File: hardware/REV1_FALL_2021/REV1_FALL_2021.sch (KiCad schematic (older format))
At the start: 5 parts

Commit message: Added annotationsto circuits
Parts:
- gave numbers to parts that had none: 5
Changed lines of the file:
@@
 $EndDescr
 $Comp
-L teensy:Teensy3.6_All_Pins U?
+L teensy:Teensy3.6_All_Pins U1
 U 1 1 6198EEB0
 P 2200 3600
-F 0 "U?" H 2200 6237 60  0000 C CNN
+F 0 "U1" H 2200 6237 60  0000 C CNN
 F 1 "Teensy3.6_All_Pins" H 2200 6131 60  0000 C CNN
 F 2 "teensy:Teensy35_36" H 2200 3650 60  0000 C CNN
@@
 $EndComp
 $Comp
-L REV1_FALL_2021-rescue:BNO055_Breakout-Sensors_2021_2022 U?
+L REV1_FALL_2021-rescue:BNO055_Breakout-Sensors_2021_2022 U4
 U 1 1 61992B5E
 P 5950 2000
-F 0 "U?" H 5950 2800 50  0000 C CNN
+F 0 "U4" H 5950 2800 50  0000 C CNN
 F 1 "BNO055_Breakout" H 5950 2700 50  0000 C CNN
 F 2 "sensors_2021_2022:BNO055_Breakout" H 5950 2750 50  0001 C CNN
@@
 $EndComp
 $Comp
-L Sensors_2021_2022:MPL3115A2_Breakout U?
+L Sensors_2021_2022:MPL3115A2_Breakout U3
 U 1 1 61994643
 P 5900 3950
-F 0 "U?" H 5850 4750 50  0000 L CNN
+F 0 "U3" H 5850 4750 50  0000 L CNN
 F 1 "MPL3115A2_Breakout" H 5500 4850 50  0000 L CNN
 F 2 "sensors_2021_2022:MPL311A2_Breakout" H 5900 4400 50  0001 C CNN
@@
 $EndComp
 $Comp
-L Sensors_2021_2022:PA16165_Breakout U?
+L Sensors_2021_2022:PA16165_Breakout U2
 U 1 1 6199B8C8
 P 5850 6000
-F 0 "U?" H 5800 6950 50  0000 L CNN
+F 0 "U2" H 5800 6950 50  0000 L CNN
 F 1 "PA16165_Breakout" H 5500 7050 50  0000 L CNN
 F 2 "sensors_2021_2022:PA16165_Breakout" H 5800 6650 50  0001 C CNN
@@
 $EndComp
 $Comp
-L Sensors_2021_2022:RFM69HCW_Breakout U?
+L Sensors_2021_2022:RFM69HCW_Breakout U5
 U 1 1 6194AAD4
 P 9050 2250
-F 0 "U?" H 9050 3298 50  0000 C CNN
+F 0 "U5" H 9050 3298 50  0000 C CNN
 F 1 "RFM69HCW_Breakout" H 9050 3207 50  0000 C CNN
 F 2 "sensors_2021_2022:RFM69HCW_Breakout" H 8900 3050 50  0001 C CNN

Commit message: Added outlines on the breakout board's footprints. Assembled PCB with wires, needs checking by Ian
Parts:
- U3: footprint sensors_2021_2022:MPL311A2_Breakout -> sensors_2021_2022:MPL3115A2_Breakout
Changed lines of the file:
@@
 F 0 "U3" H 5850 4750 50  0000 L CNN
 F 1 "MPL3115A2_Breakout" H 5500 4850 50  0000 L CNN
-F 2 "sensors_2021_2022:MPL311A2_Breakout" H 5900 4400 50  0001 C CNN
+F 2 "sensors_2021_2022:MPL3115A2_Breakout" H 5900 4400 50  0001 C CNN
 F 3 "" H 5900 4400 50  0001 C CNN
 	1    5900 3950
@@
 F 3 "" H 5800 6650 50  0001 C CNN
 	1    5850 6000
-	1    0    0    -1
-$EndComp
-$Comp
-L Sensors_2021_2022:RFM69HCW_Breakout U5
-U 1 1 6194AAD4
-P 9050 2250
-F 0 "U5" H 9050 3298 50  0000 C CNN
-F 1 "RFM69HCW_Breakout" H 9050 3207 50  0000 C CNN
-F 2 "sensors_2021_2022:RFM69HCW_Breakout" H 8900 3050 50  0001 C CNN
-F 3 "" H 8900 3050 50  0001 C CNN
-	1    9050 2250
 	1    0    0    -1
 $EndComp
@@
 NoConn ~ 9400 1800
 NoConn ~ 9400 1650
+$Comp
+L Sensors_2021_2022:RFM69HCW_Breakout U5
+U 1 1 6194AAD4
+P 9050 2250
+F 0 "U5" H 9050 3298 50  0000 C CNN
+F 1 "RFM69HCW_Breakout" H 9050 3207 50  0000 C CNN
+F 2 "sensors_2021_2022:RFM69HCW_Breakout" H 8900 3050 50  0001 C CNN
+F 3 "" H 8900 3050 50  0001 C CNN
+	1    9050 2250
+	1    0    0    -1
+$EndComp
 $EndSCHEMATC

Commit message: Verify pin connections on layout and fix mistakes
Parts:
- U4: symbol REV1_FALL_2021-rescue:BNO055_Breakout-Sensors_2021_2022 -> Sensors_2021_2022:BNO055_Breakout
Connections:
- wire segments 32 -> 36
- no-connect marks 96 -> 91
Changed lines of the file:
@@
 $EndComp
 $Comp
-L REV1_FALL_2021-rescue:BNO055_Breakout-Sensors_2021_2022 U4
+L Sensors_2021_2022:BNO055_Breakout U4
 U 1 1 61992B5E
 P 5950 2000
@@
 	1    0    0    -1
 $EndComp
-$Comp
-L Sensors_2021_2022:PA16165_Breakout U2
-U 1 1 6199B8C8
-P 5850 6000
-F 0 "U2" H 5800 6950 50  0000 L CNN
-F 1 "PA16165_Breakout" H 5500 7050 50  0000 L CNN
-F 2 "sensors_2021_2022:PA16165_Breakout" H 5800 6650 50  0001 C CNN
-F 3 "" H 5800 6650 50  0001 C CNN
-	1    5850 6000
-	1    0    0    -1
-$EndComp
-Text Label 3650 2550 0    50   ~ 0
+Text Label 3600 5150 0    50   ~ 0
 3.3V
 Text Label 5300 1650 0    50   ~ 0
@@
 Text Label 5350 3500 0    50   ~ 0
 3.3V
-Text Label 5300 5400 0    50   ~ 0
+Text Label 5300 6450 0    50   ~ 0
 3.3V
 Text Label 8400 1650 0    50   ~ 0
 3.3V
-Text Label 3650 2650 0    50   ~ 0
-GND
-Text Label 5300 1800 0    50   ~ 0
+Text Label 900  5250 2    50   ~ 0
+GND
+Text Label 5300 1950 0    50   ~ 0
 GND
 Text Label 5350 3650 0    50   ~ 0
@@
 Text Label 5350 4400 0    50   ~ 0
 SDA0
+Text Label 5300 2100 0    50   ~ 0
+SDA0
 Text Label 5300 2250 0    50   ~ 0
-SDA0
-Text Label 5300 2100 0    50   ~ 0
 SCL0
 Text Label 5350 4250 0    50   ~ 0
@@
 	5600 1650 5300 1650
 Wire Wire Line
-	5300 1800 5600 1800
-Wire Wire Line
 	5600 2100 5300 2100
 Wire Wire Line
@@
 	5650 4400 5350 4400
 Wire Wire Line
-	5300 5400 5600 5400
-Wire Wire Line
 	5600 6000 5300 6000
 Wire Wire Line
@@
 Wire Wire Line
 	8400 2850 8700 2850
-NoConn ~ 1050 1450
 NoConn ~ 1050 1950
 NoConn ~ 1050 2050
@@
 NoConn ~ 1050 2350
 NoConn ~ 1050 2450
-NoConn ~ 1050 2850
 NoConn ~ 1050 2950
 NoConn ~ 1050 3050
@@
 NoConn ~ 1050 5050
 NoConn ~ 1050 5150
-NoConn ~ 1050 5250
 NoConn ~ 1050 5450
 NoConn ~ 1050 5550
@@
 NoConn ~ 3350 5350
 NoConn ~ 3350 5250
-NoConn ~ 3350 5150
 NoConn ~ 3350 5050
 NoConn ~ 3350 4950
@@
 NoConn ~ 6300 2100
 NoConn ~ 6300 2250
-NoConn ~ 5600 1950
 NoConn ~ 5600 2400
 NoConn ~ 5650 3800
@@
 NoConn ~ 5600 5700
 NoConn ~ 5600 5850
-NoConn ~ 5600 6450
 NoConn ~ 5600 6600
 NoConn ~ 8700 1950
@@
 	1    0    0    -1
 $EndComp
+$Comp
+L Sensors_2021_2022:PA16165_Breakout U2
+U 1 1 6199B8C8
+P 5850 6000
+F 0 "U2" H 5800 6950 50  0000 L CNN
+F 1 "PA16165_Breakout" H 5500 7050 50  0000 L CNN
+F 2 "sensors_2021_2022:PA16165_Breakout" H 5800 6650 50  0001 C CNN
+F 3 "" H 5800 6650 50  0001 C CNN
+	1    5850 6000
+	1    0    0    -1
+$EndComp
+Wire Wire Line
+	5600 6450 5300 6450
+NoConn ~ 5600 5400
+Wire Wire Line
+	5600 1950 5300 1950
+Wire Wire Line
+	3350 5150 3600 5150
+Wire Wire Line
+	1050 5250 900  5250
+Text Label 900  1450 2    50   ~ 0
+GND
+Wire Wire Line
+	1050 1450 900  1450
+Text Label 750  2850 0    50   ~ 0
+3.3V
+Wire Wire Line
+	1050 2850 750  2850
 $EndSCHEMATC

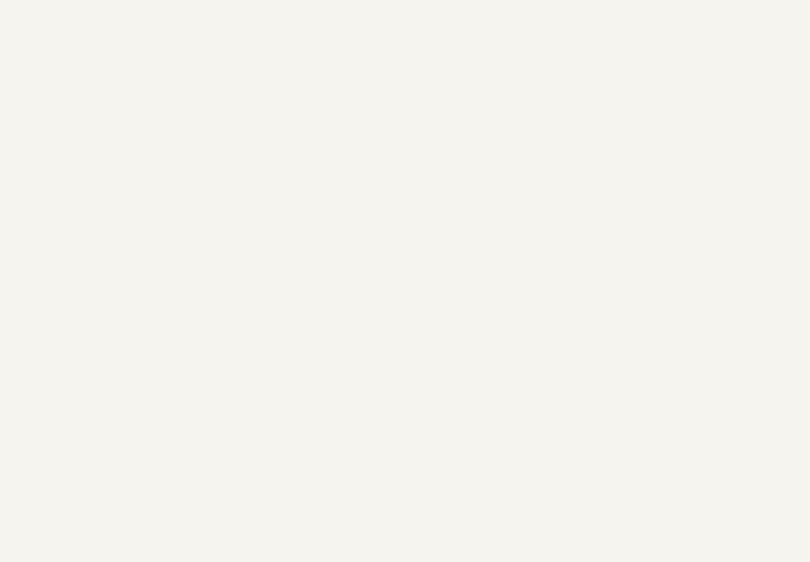
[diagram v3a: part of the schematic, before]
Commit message: add power switcher (no traces connected yet)
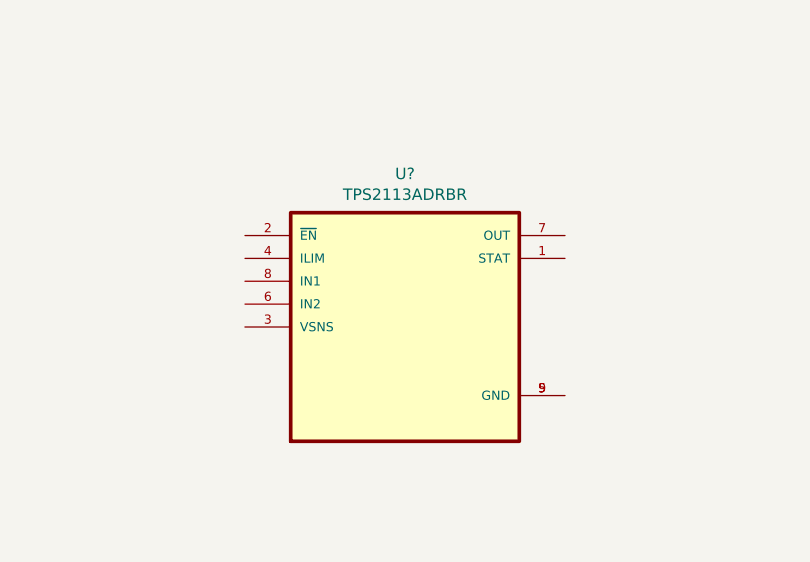
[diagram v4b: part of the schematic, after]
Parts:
- added U?: TPS2113ADRBR, IC_DRV8601DRBT, symbol TPS2113ADRBR:TPS2113ADRBR
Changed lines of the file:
@@
 Wire Wire Line
 	1050 2850 750  2850
+$Comp
+L TPS2113ADRBR:TPS2113ADRBR U?
+U 1 1 6198C58A
+P 9550 5800
+F 0 "U?" H 9550 6470 50  0000 C CNN
+F 1 "TPS2113ADRBR" H 9550 6379 50  0000 C CNN
+F 2 "IC_DRV8601DRBT" H 9550 5800 50  0001 L BNN
+F 3 "" H 9550 5800 50  0001 L BNN
+	1    9550 5800
+	1    0    0    -1
+$EndComp
 $EndSCHEMATC

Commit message: WIP adding TPS2113A
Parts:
- added BT? (x2): Battery_Cell, symbol Device:Battery_Cell
- added C? (x2): C, symbol Device:C
- added R? (x2): R, symbol Device:R
- added R?: 15k, symbol Device:R
- added R?: 5k, symbol Device:R
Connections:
- net labels added: SWITCH, VIN
- wire segments 36 -> 76
- no-connect marks 91 -> 89
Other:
- moved on the sheet: U?

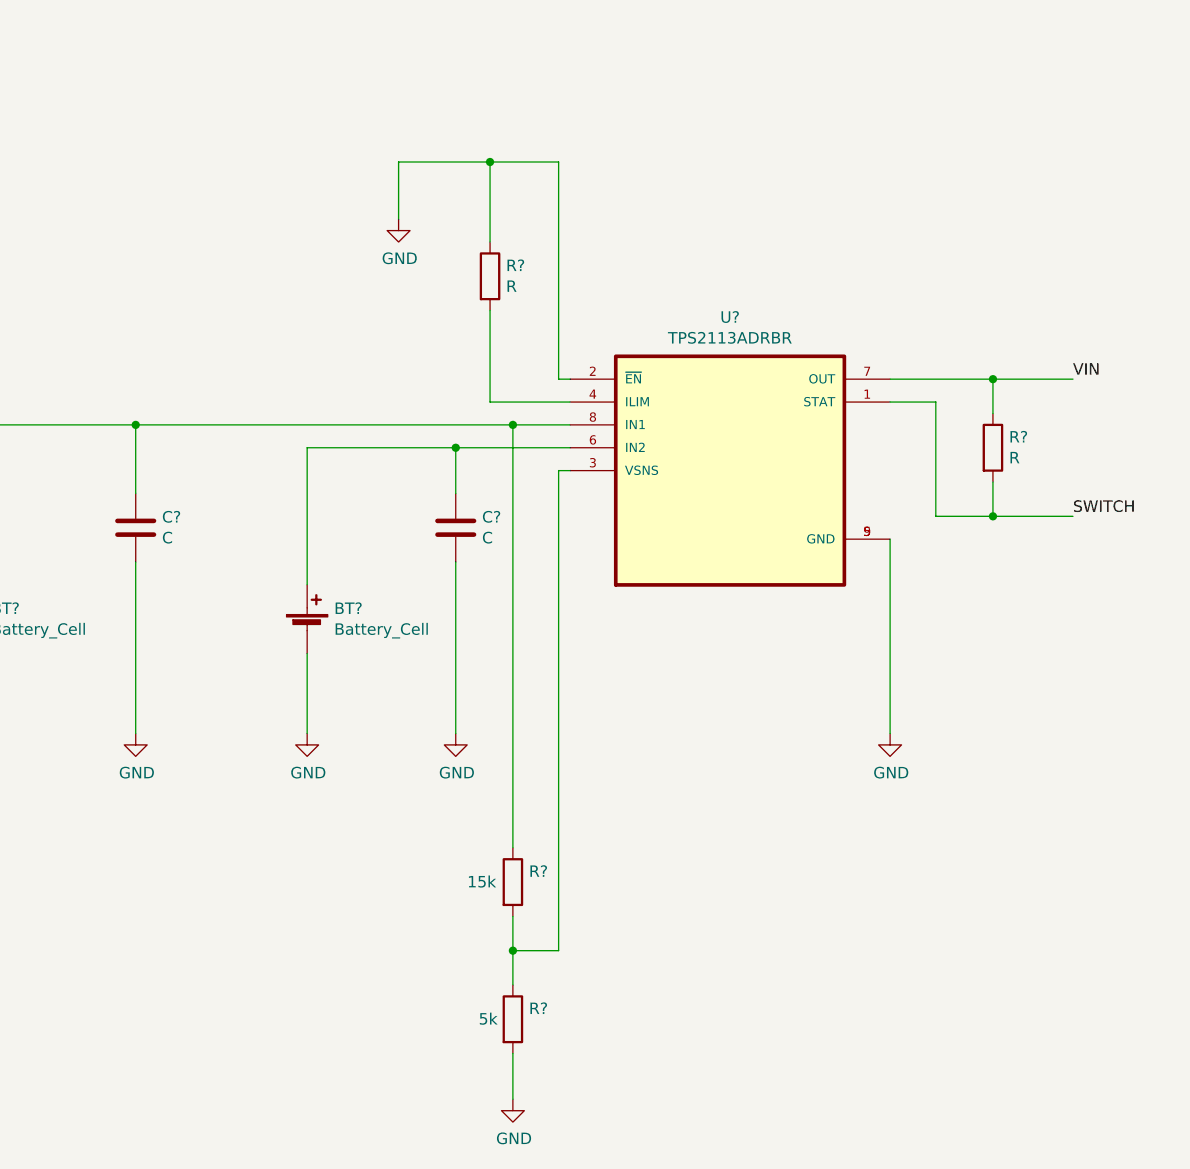
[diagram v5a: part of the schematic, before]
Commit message: finish TPS2113A schematic
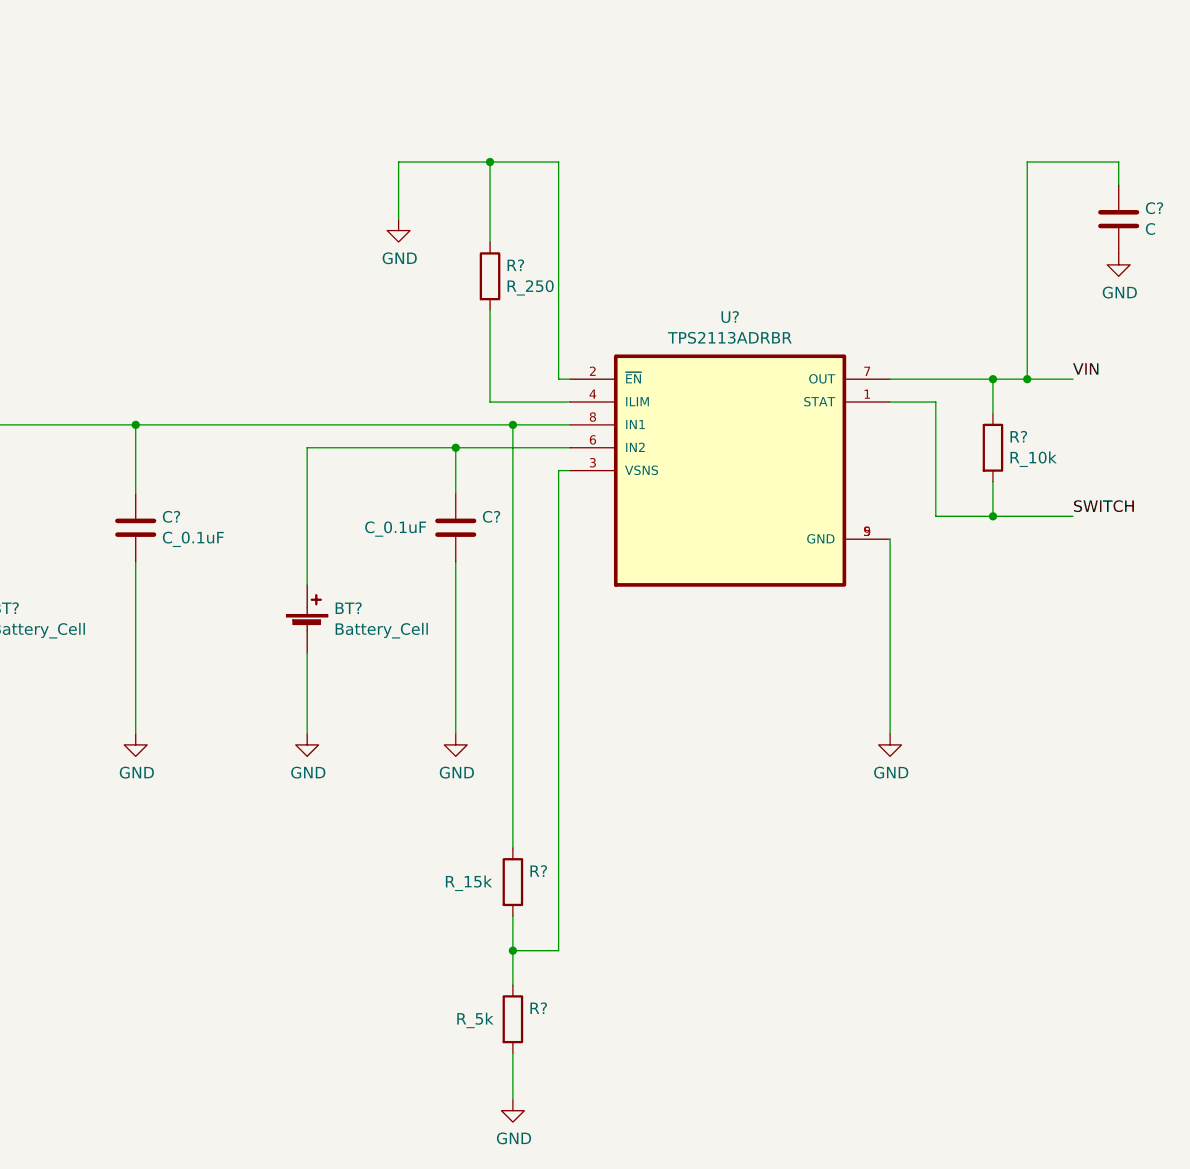
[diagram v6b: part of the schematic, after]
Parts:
- added C?: C, symbol Device:C
- C? (x2): value C -> C_0.1uF
- R?: value R -> R_250
- R?: value 15k -> R_15k
- R?: value 5k -> R_5k
- R?: value R -> R_10k
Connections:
- net GND: now also C?.2
- net VIN: now also C?.1
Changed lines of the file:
@@
 P 13750 5600
 F 0 "C?" H 13865 5646 50  0000 L CNN
-F 1 "C" H 13865 5555 50  0000 L CNN
+F 1 "C_0.1uF" H 13865 5555 50  0000 L CNN
 F 2 "" H 13788 5450 50  0001 C CNN
 F 3 "~" H 13750 5600 50  0001 C CNN
@@
 P 15150 5600
 F 0 "C?" H 15265 5646 50  0000 L CNN
-F 1 "C" H 15265 5555 50  0000 L CNN
+F 1 "C_0.1uF" H 14750 5600 50  0000 L CNN
 F 2 "" H 15188 5450 50  0001 C CNN
 F 3 "~" H 15150 5600 50  0001 C CNN
@@
 P 15300 4500
 F 0 "R?" H 15370 4546 50  0000 L CNN
-F 1 "R" H 15370 4455 50  0000 L CNN
+F 1 "R_250" H 15370 4455 50  0000 L CNN
 F 2 "" V 15230 4500 50  0001 C CNN
 F 3 "~" H 15300 4500 50  0001 C CNN
@@
 P 15400 7150
 F 0 "R?" H 15470 7196 50  0000 L CNN
-F 1 "15k" H 15200 7150 50  0000 L CNN
+F 1 "R_15k" H 15100 7150 50  0000 L CNN
 F 2 "" V 15330 7150 50  0001 C CNN
 F 3 "~" H 15400 7150 50  0001 C CNN
@@
 P 15400 7750
 F 0 "R?" H 15470 7796 50  0000 L CNN
-F 1 "5k" H 15250 7750 50  0000 L CNN
+F 1 "R_5k" H 15150 7750 50  0000 L CNN
 F 2 "" V 15330 7750 50  0001 C CNN
 F 3 "~" H 15400 7750 50  0001 C CNN
@@
 P 17500 5250
 F 0 "R?" H 17570 5296 50  0000 L CNN
-F 1 "R" H 17570 5205 50  0000 L CNN
+F 1 "R_10k" H 17570 5205 50  0000 L CNN
 F 2 "" V 17430 5250 50  0001 C CNN
 F 3 "~" H 17500 5250 50  0001 C CNN
@@
 	17500 5100 17500 4950
 Connection ~ 17500 4950
-Wire Wire Line
-	17500 4950 17850 4950
 Text Label 17850 5550 0    50   ~ 0
 SWITCH
@@
 Wire Wire Line
 	650  4550 1050 4550
+$Comp
+L Device:C C?
+U 1 1 619DA45A
+P 18050 4250
+F 0 "C?" H 18165 4296 50  0000 L CNN
+F 1 "C" H 18165 4205 50  0000 L CNN
+F 2 "" H 18088 4100 50  0001 C CNN
+F 3 "~" H 18050 4250 50  0001 C CNN
+	1    18050 4250
+	1    0    0    -1
+$EndComp
+Wire Wire Line
+	17500 4950 17650 4950
+Wire Wire Line
+	17650 4950 17650 4000
+Wire Wire Line
+	17650 4000 18050 4000
+Wire Wire Line
+	18050 4000 18050 4100
+Connection ~ 17650 4950
+Wire Wire Line
+	17650 4950 17850 4950
+$Comp
+L power:GND #PWR?
+U 1 1 619E2365
+P 18050 4400
+F 0 "#PWR?" H 18050 4150 50  0001 C CNN
+F 1 "GND" H 18055 4227 50  0000 C CNN
+F 2 "" H 18050 4400 50  0001 C CNN
+F 3 "" H 18050 4400 50  0001 C CNN
+	1    18050 4400
+	1    0    0    -1
+$EndComp
 $EndSCHEMATC

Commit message: WIP adding second TPS2113A
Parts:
- added BT? (x2): Battery_Cell, symbol Device:Battery_Cell
- added J?: Screw_Terminal_01x02, symbol Connector:Screw_Terminal_01x02
- added Q?: Q_NMOS_GDS, footprints:TO-220-3, symbol Device:Q_NMOS_GDS
- added R?: R_15k, symbol Device:R
- added R?: R_5k, symbol Device:R
- added R?: R_10k, symbol Device:R
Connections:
- net GND: now also BT?.2 (-), BT?.2 (-), Q?.3 (S), R?.2
- net SWITCH renamed STAT
- new net: Q?.1 (G), R?.1
- new net: J?.2 (Pin_2), Q?.2 (D)
- new net E-Match_Trigger_1: R?.2
- new net TPS2113A for E-match/IN1: BT?.1 (+), R?.1
- new net TPS2113A for E-match/IN2: BT?.1 (+)
- new net TPS2113A for Teensy power/VSNS: R?.1, R?.2
- new net V_EMATCH: J?.1 (Pin_1)
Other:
- note added: "E-Match in series here"

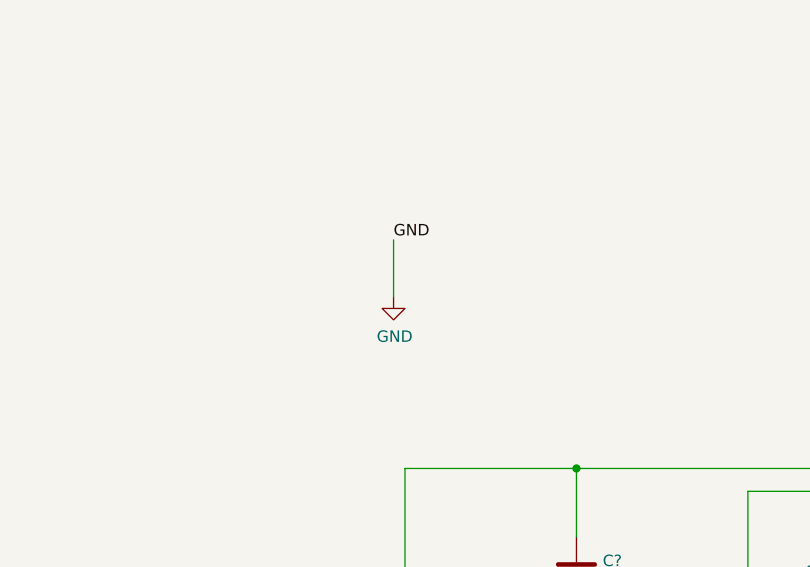
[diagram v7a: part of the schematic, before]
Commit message: fix hierarchical sheet duplicates
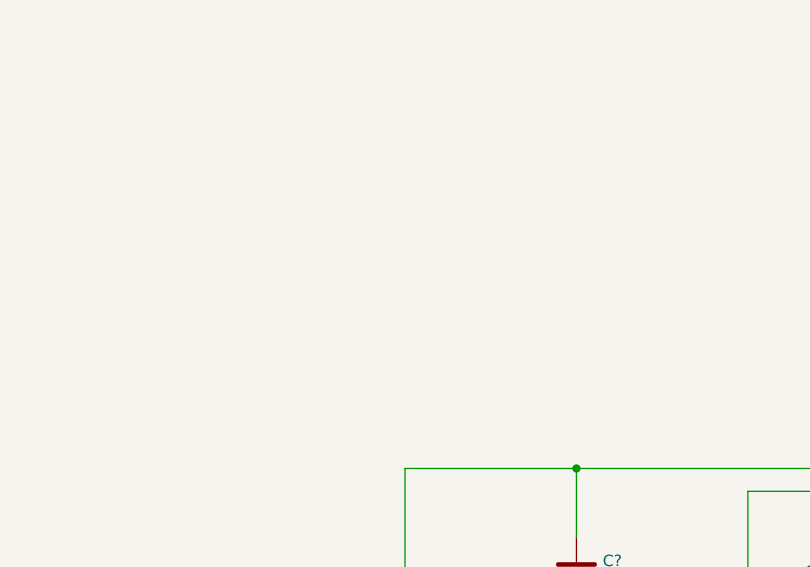
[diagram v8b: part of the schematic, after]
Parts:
- J?: footprint (none) -> TerminalBlock:TerminalBlock_bornier-2_P5.08mm
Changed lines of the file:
@@
 	1    0    0    -1
 $EndComp
-$Comp
-L power:GND #PWR?
-U 1 1 619B0F8C
-P 12950 4400
-F 0 "#PWR?" H 12950 4150 50  0001 C CNN
-F 1 "GND" H 12955 4227 50  0000 C CNN
-F 2 "" H 12950 4400 50  0001 C CNN
-F 3 "" H 12950 4400 50  0001 C CNN
-	1    12950 4400
-	1    0    0    -1
-$EndComp
-Wire Wire Line
-	12950 4400 12950 4150
-Text Label 12950 4150 0    50   ~ 0
-GND
 Wire Wire Line
 	15650 5350 15600 5350
@@
 F 0 "J?" H 17030 9292 50  0000 L CNN
 F 1 "Screw_Terminal_01x02" H 17030 9201 50  0000 L CNN
-F 2 "" H 16950 9300 50  0001 C CNN
+F 2 "TerminalBlock:TerminalBlock_bornier-2_P5.08mm" H 16950 9300 50  0001 C CNN
 F 3 "~" H 16950 9300 50  0001 C CNN
 	1    16950 9300
